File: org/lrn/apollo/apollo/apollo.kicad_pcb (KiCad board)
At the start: 2 copper layers, 72 parts, among them J10 Conn_01x01_Male, J11 Conn_01x01_Male, J12 Conn_01x01_Male, J13 Conn_01x01_Male, J17 Conn_01x01_Male, J18 Conn_01x01_Male, J4 Conn_01x01_Male, J6 Conn_01x01_Male, J7 Conn_01x01_Male, J8 Conn_01x01_Male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

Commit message: apollo: checkpoint
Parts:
- moved J_GND1 140.4 mm to (19.8, 19.8)
- moved JH_9 102.0 mm to (28.0, 94.0)
- moved J8 75.0 mm to (67.7, 58.5)
- moved U4 75.0 mm to (72.8, 68.7)
- moved D1 75.0 mm to (31.7, 27.4)
- moved D2 75.0 mm to (23.6, 34.2)
- moved D3 75.0 mm to (42.3, 34.2)
- moved D4 75.0 mm to (50.5, 27.4)
- moved D_RED_1 75.0 mm to (19.8, 42.8)
- moved J6 75.0 mm to (72.8, 57.5)
- moved J7 75.0 mm to (70.2, 62.8)
- moved JA_15 75.0 mm to (19.0, 63.2)
- moved JC_2 75.0 mm to (19.0, 68.2)
- moved JD_3 75.0 mm to (18.9, 70.8)
- moved JE_4 75.0 mm to (18.9, 73.3)
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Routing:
- net GND: track 452.3 -> 504.3 mm, vias 3 -> 1
- net Net-(JH_2-Pad1): track 131.8 -> 142.9 mm
- net VCC: track 462.8 -> 473.1 mm
- net Net-(JH_3-Pad1): track 145.9 -> 152.7 mm, vias 2 -> 0

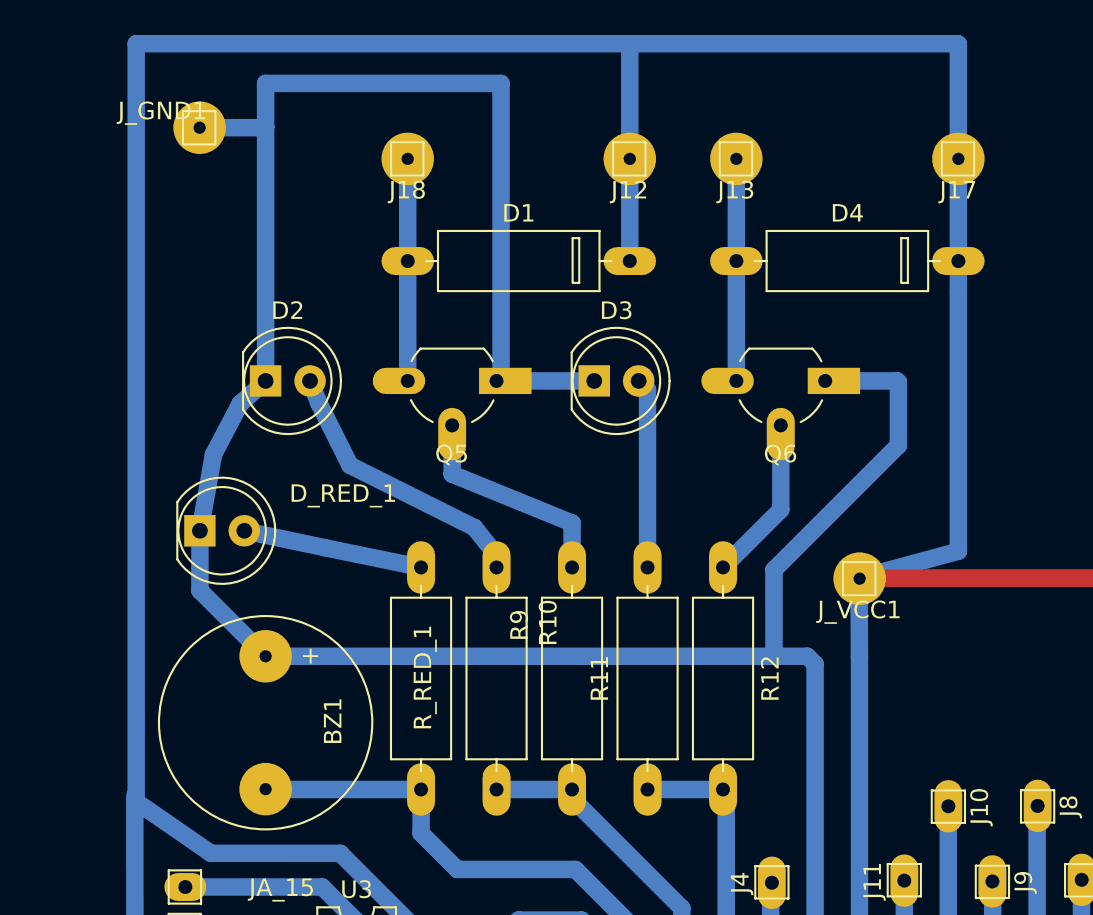
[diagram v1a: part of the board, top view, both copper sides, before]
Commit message: apollo:scheme micro usb connector for vcc and gnd
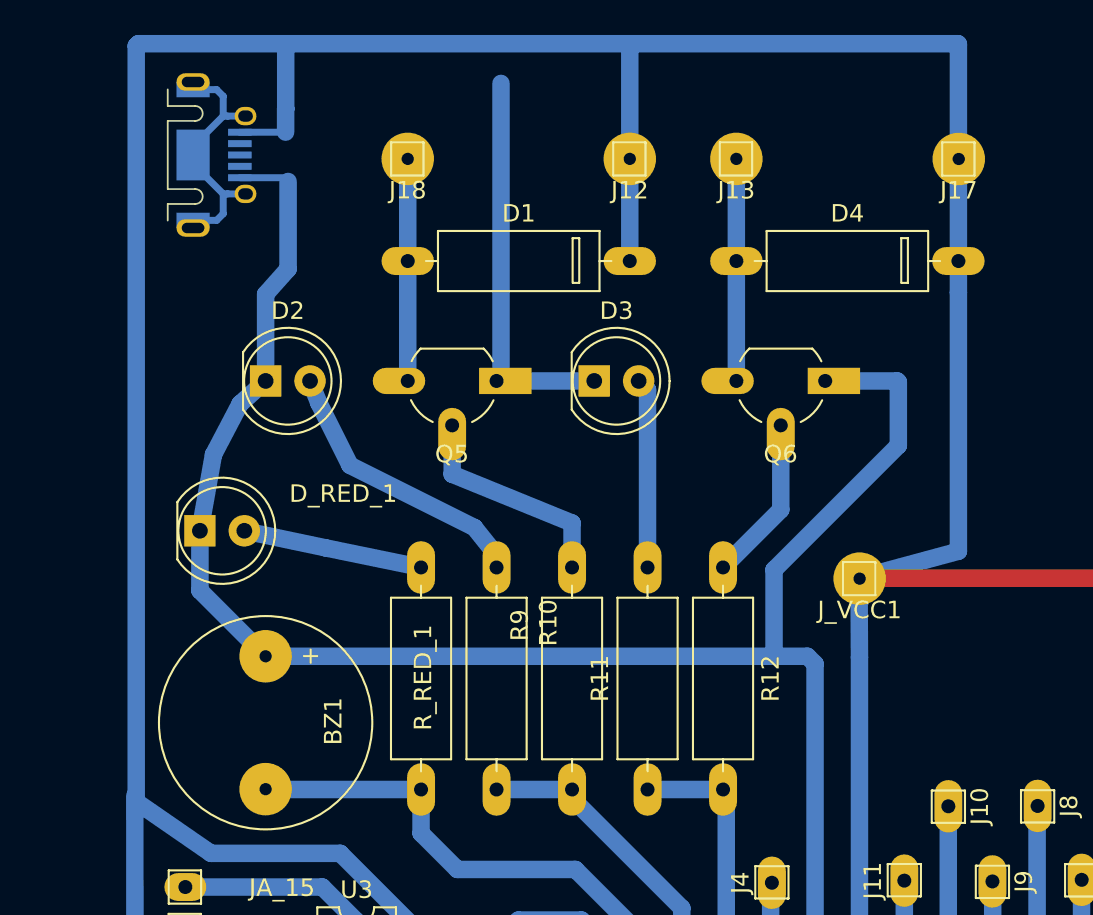
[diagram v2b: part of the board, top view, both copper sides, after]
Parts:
- removed the J_GND1 at (19.8, 19.8)
- added J_USB_1: USB_B_Micro, Connector_USB:USB_Micro-AB_Molex_47590-0001, B.Cu at (19.4, 21.3)
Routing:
- net GND: track 504.3 -> 484.5 mm
- net Net-(J_USB_1-Pad6): track 0.00 -> 14.5 mm
- net VCC: track 473.1 -> 480.7 mm
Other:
- board outline added: 2 x 7.5 mm
- net class Default: clearance 0.8 -> 0.6
- net class Micro added: clearance 0.2, trace_width 0.3, via_dia 0.5, via_drill 0.4
- rule trace_clearance: 0.8 -> 0.6

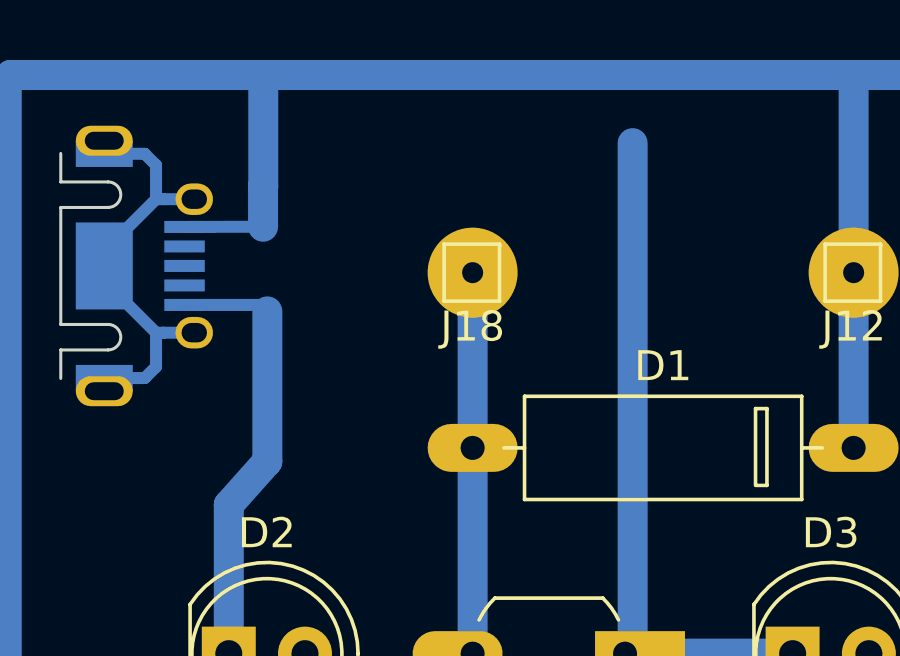
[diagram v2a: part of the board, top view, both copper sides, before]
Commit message: apollo: fix gnd track and prepare to use 9 pin
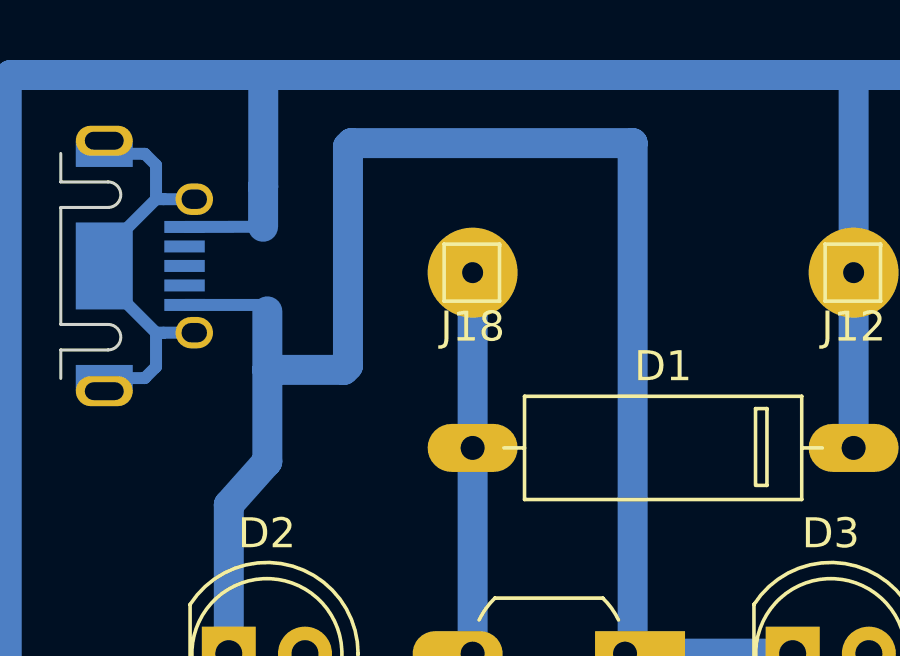
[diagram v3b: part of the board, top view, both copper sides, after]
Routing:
- net GND: track 484.5 -> 504.1 mm
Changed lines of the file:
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@@
     (thickness 1.6)
     (drawings 0)
-    (tracks 392)
+    (tracks 398)
     (zones 0)
     (modules 72)
@@
   (segment (start 23.55088 29.27604) (end 24.83612 27.83332) (width 1) (layer B.Cu) (net 26))
   (segment (start 23.55088 34.2392) (end 23.55088 29.27604) (width 1) (layer B.Cu) (net 26))
-  (segment (start 24.83612 27.83332) (end 24.83612 22.82952) (width 1) (layer B.Cu) (net 26))
+  (segment (start 24.83612 24.78024) (end 27.38628 24.78024) (width 1) (layer B.Cu) (net 26))
+  (segment (start 24.83612 27.83332) (end 24.83612 24.78024) (width 1) (layer B.Cu) (net 26))
+  (segment (start 24.83612 24.78024) (end 24.83612 22.82952) (width 1) (layer B.Cu) (net 26))
+  (segment (start 27.38628 24.78024) (end 27.52344 24.64308) (width 1) (layer B.Cu) (net 26))
+  (segment (start 27.52344 24.64308) (end 27.52344 17.33804) (width 1) (layer B.Cu) (net 26))
+  (segment (start 27.64028 17.2212) (end 27.52344 17.33804) (width 1) (layer B.Cu) (net 26))
+  (segment (start 37.01288 17.2212) (end 27.64028 17.2212) (width 1) (layer B.Cu) (net 26))
   (segment (start 32.564601 80.914441) (end 32.890661 80.914441) (width 1) (layer F.Cu) (net 27))
   (segment (start 32.575299 65.674441) (end 32.564601 65.674441) (width 1) (layer F.Cu) (net 27))

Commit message: apollo: remove wrong junctions
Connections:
- JA_15 pad 1: VCC -> Net-(JA_15-Pad1)
- JB_1 pad 1: VCC -> Net-(JB_1-Pad1)
- JC_2 pad 1: VCC -> Net-(JC_2-Pad1)
- JD_3 pad 1: VCC -> Net-(JD_3-Pad1)
- JE_4 pad 1: VCC -> Net-(JE_4-Pad1)
- JF_5 pad 1: VCC -> Net-(JF_5-Pad1)
- JG_6 pad 1: VCC -> Net-(JG_6-Pad1)
- JH_7 pad 1: VCC -> Net-(JH_7-Pad1)
- U3 pad 1: VCC -> Net-(JB_1-Pad1)
- U3 pad 15: VCC -> Net-(JA_15-Pad1)
- U3 pad 2: VCC -> Net-(JC_2-Pad1)
- U3 pad 3: VCC -> Net-(JD_3-Pad1)
- U3 pad 4: VCC -> Net-(JE_4-Pad1)
- U3 pad 5: VCC -> Net-(JF_5-Pad1)
- U3 pad 6: VCC -> Net-(JG_6-Pad1)
- U3 pad 7: VCC -> Net-(JH_7-Pad1)
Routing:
- net VCC: track 480.7 -> 421.2 mm
- net Net-(JA_15-Pad1): track 0.00 -> 17.5 mm
- net Net-(JE_4-Pad1): track 0.00 -> 6.08 mm
- net Net-(JD_3-Pad1): track 0.00 -> 6.01 mm
- net Net-(JF_5-Pad1): track 0.00 -> 6.01 mm
- net Net-(JB_1-Pad1): track 0.00 -> 6.00 mm
- net Net-(JC_2-Pad1): track 0.00 -> 6.00 mm
- net Net-(JH_7-Pad1): track 0.00 -> 6.00 mm
- net Net-(JG_6-Pad1): track 0.00 -> 5.97 mm

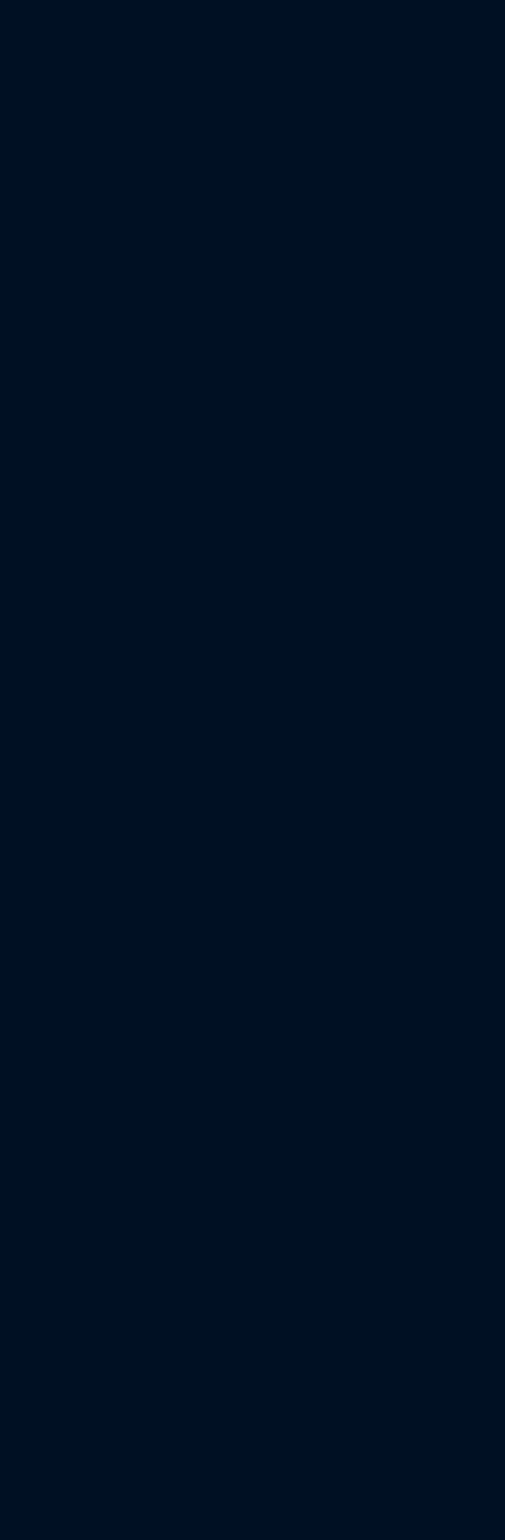
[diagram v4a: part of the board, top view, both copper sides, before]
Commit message: apollo: keybard added
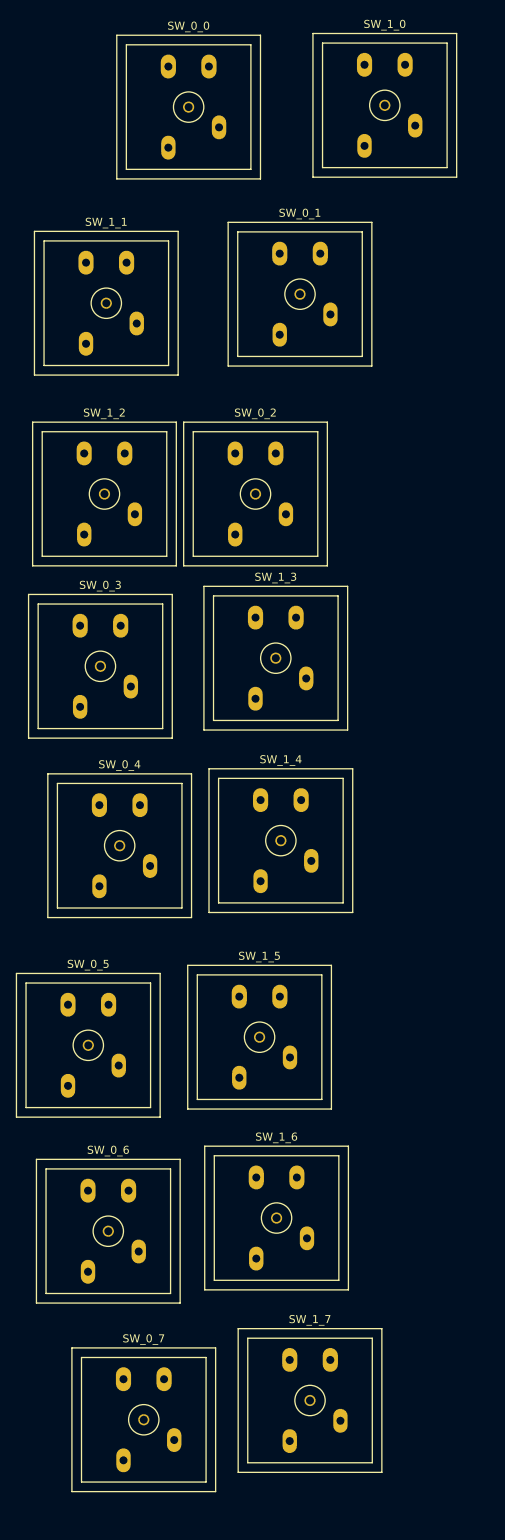
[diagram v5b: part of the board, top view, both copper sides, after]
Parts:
- added SW_0_0: SW_SPST_DIODE, apollo:gateron, F.Cu at (-31.2, -11.6)
- added SW_0_1: SW_SPST_DIODE, apollo:gateron, F.Cu at (-17.2, 11.9)
- added SW_0_2: SW_SPST_DIODE, apollo:gateron, F.Cu at (-22.8, 36.9)
- added SW_0_3: SW_SPST_DIODE, apollo:gateron, F.Cu at (-42.2, 58.5)
- added SW_0_4: SW_SPST_DIODE, apollo:gateron, F.Cu at (-39.8, 81.0)
- added SW_0_5: SW_SPST_DIODE, apollo:gateron, F.Cu at (-43.7, 106.0)
- added SW_0_6: SW_SPST_DIODE, apollo:gateron, F.Cu at (-41.2, 129.3)
- added SW_0_7: SW_SPST_DIODE, apollo:gateron, F.Cu at (-36.8, 152.9)
- added SW_1_0: SW_SPST_DIODE, apollo:gateron, F.Cu at (-6.61, -11.8)
- added SW_1_1: SW_SPST_DIODE, apollo:gateron, F.Cu at (-41.5, 13.0)
- added SW_1_2: SW_SPST_DIODE, apollo:gateron, F.Cu at (-41.7, 36.9)
- added SW_1_3: SW_SPST_DIODE, apollo:gateron, F.Cu at (-20.3, 57.5)
- added SW_1_4: SW_SPST_DIODE, apollo:gateron, F.Cu at (-19.6, 80.3)
- added SW_1_5: SW_SPST_DIODE, apollo:gateron, F.Cu at (-22.3, 104.9)
- added SW_1_6: SW_SPST_DIODE, apollo:gateron, F.Cu at (-20.2, 127.6)
- added SW_1_7: SW_SPST_DIODE, apollo:gateron, F.Cu at (-16.0, 150.5)
